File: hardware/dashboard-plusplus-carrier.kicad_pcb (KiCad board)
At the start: 4 copper layers, 95 x 55 mm, 54 parts, among them J1 XT30U-M, J10a ESP32-DEVKIT-A, J10b ESP32-DEVKIT-B, J13 DEBUG, J14 TRIP + EN, J15 SPARE, J17 IGN + COOLANT, J3 TFT-ILI9488, J6 LDR + FUEL, J8 GPS_PADS, J9 HALL, Q1 IRFR9540N, U4 DPP_DCDC_MODULE

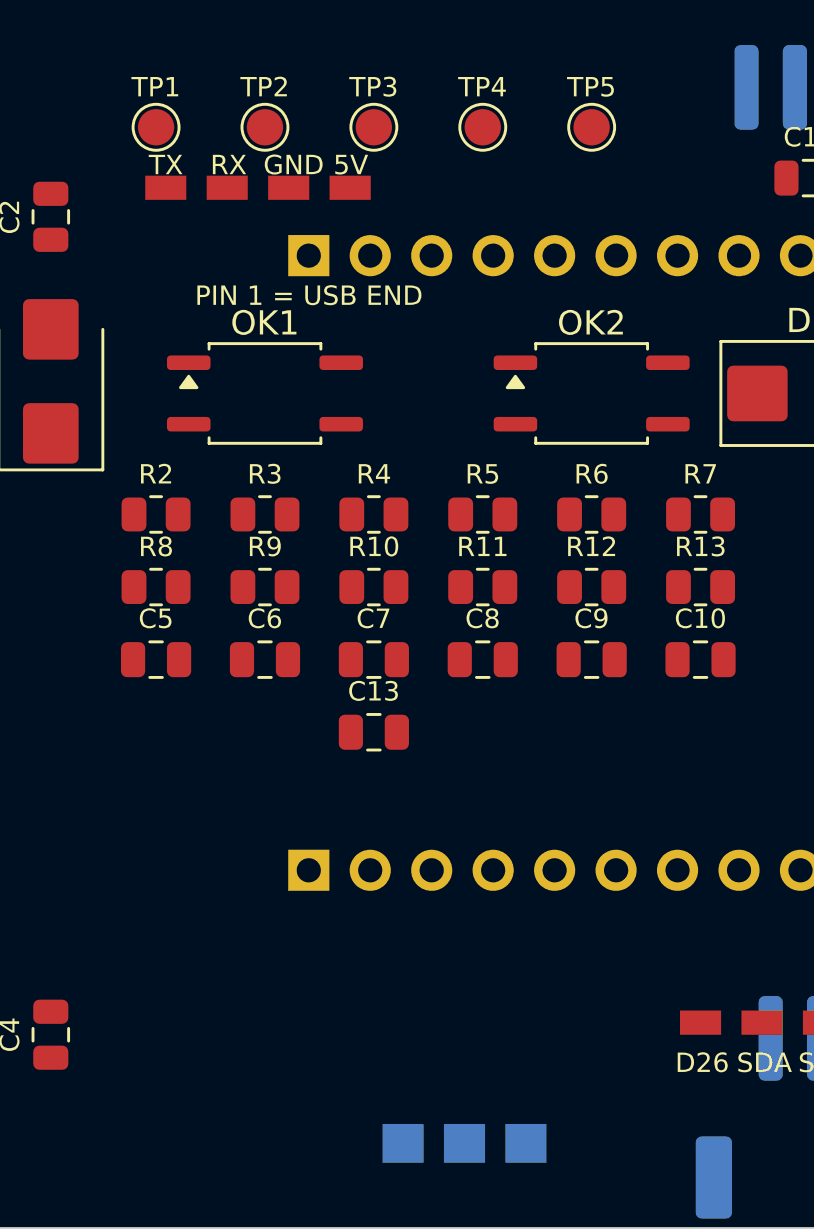
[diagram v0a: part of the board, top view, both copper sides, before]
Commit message: Move the debug TX/RX/GND/5V pads to the spare row by D26
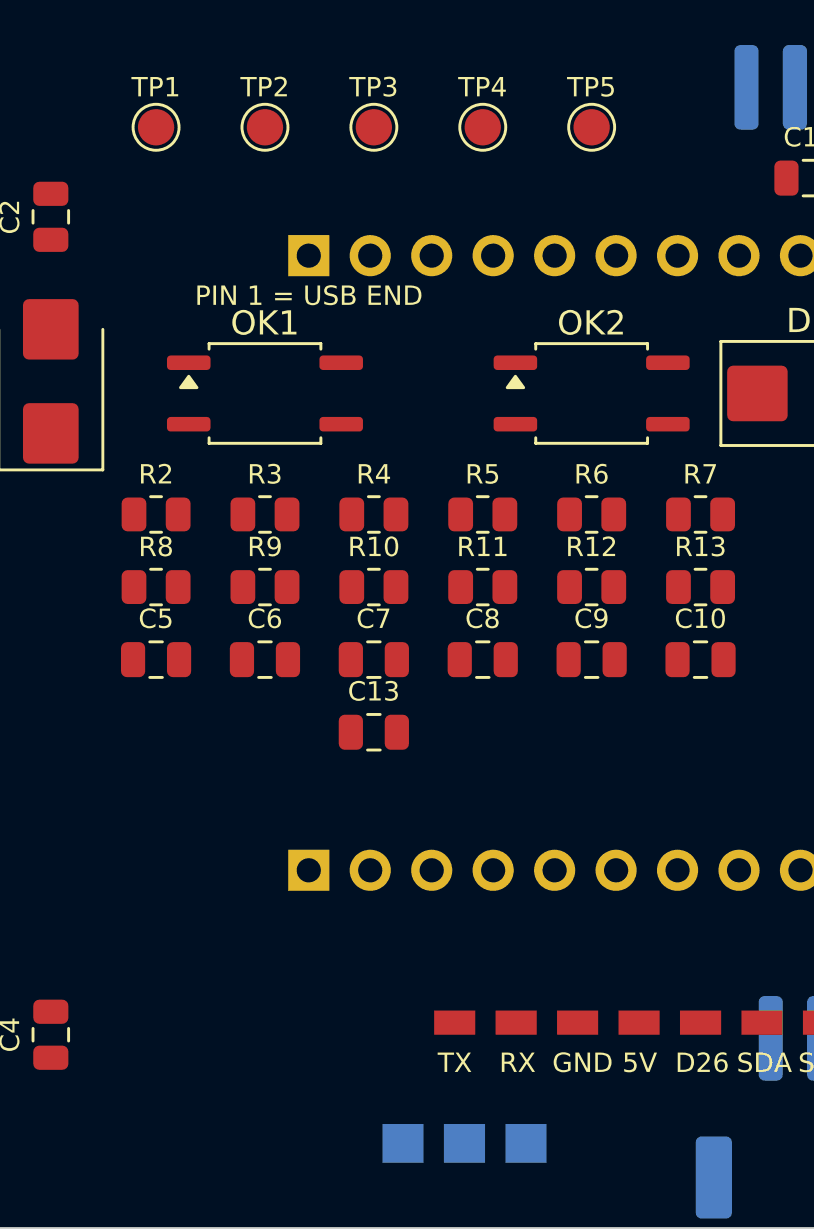
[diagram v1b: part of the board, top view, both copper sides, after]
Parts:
- moved J13 36.5 mm to (152.9, 124.0)
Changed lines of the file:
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@@
 (footprint "dpp:DEBUG"
 	(layer "F.Cu")
-	(at 141.0000 89.5000 0.0)
+	(at 152.9400 124.0000 0.0)
 	(property "Reference" "J13" (at 0.00 -1.30 0.0) (layer "F.Fab") (effects (font (size 1.0 1.0) (thickness 0.15))))
 	(property "Value" "DEBUG" (at 0.00 1.30 0.0) (layer "F.Fab") (effects (font (size 1.0 1.0) (thickness 0.15))))
@@
 (gr_text "SEL" (at 154.39 126.39 0.0) (layer "B.SilkS") (effects (font (size 0.80 0.80) (thickness 0.12)) (justify left top mirror)))
 (gr_text "12V" (at 156.94 126.39 0.0) (layer "B.SilkS") (effects (font (size 0.80 0.80) (thickness 0.12)) (justify left top mirror)))
-(gr_text "TX" (at 140.30 88.10 0.0) (layer "F.SilkS") (effects (font (size 0.80 0.80) (thickness 0.12)) (justify left top)))
-(gr_text "RX" (at 142.84 88.10 0.0) (layer "F.SilkS") (effects (font (size 0.80 0.80) (thickness 0.12)) (justify left top)))
-(gr_text "GND" (at 145.03 88.10 0.0) (layer "F.SilkS") (effects (font (size 0.80 0.80) (thickness 0.12)) (justify left top)))
-(gr_text "5V" (at 147.92 88.10 0.0) (layer "F.SilkS") (effects (font (size 0.80 0.80) (thickness 0.12)) (justify left top)))
+(gr_text "TX" (at 152.24 125.20 0.0) (layer "F.SilkS") (effects (font (size 0.80 0.80) (thickness 0.12)) (justify left top)))
+(gr_text "RX" (at 154.78 125.20 0.0) (layer "F.SilkS") (effects (font (size 0.80 0.80) (thickness 0.12)) (justify left top)))
+(gr_text "GND" (at 156.97 125.20 0.0) (layer "F.SilkS") (effects (font (size 0.80 0.80) (thickness 0.12)) (justify left top)))
+(gr_text "5V" (at 159.86 125.20 0.0) (layer "F.SilkS") (effects (font (size 0.80 0.80) (thickness 0.12)) (justify left top)))
 (gr_text "D26" (at 162.05 125.20 0.0) (layer "F.SilkS") (effects (font (size 0.80 0.80) (thickness 0.12)) (justify left top)))
 (gr_text "SDA" (at 164.59 125.20 0.0) (layer "F.SilkS") (effects (font (size 0.80 0.80) (thickness 0.12)) (justify left top)))

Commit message: Put the test-point row on the XT30 pad line (y 13.99)
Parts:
- moved TP1 5.51 mm to (140.6, 81.5)
- moved TP2 5.51 mm to (145.1, 81.5)
- moved TP3 5.51 mm to (149.6, 81.5)
- moved TP4 5.51 mm to (154.1, 81.5)
- moved TP5 5.51 mm to (158.6, 81.5)
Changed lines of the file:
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@@
 (footprint "dpp:TestPoint_Pad_D1.5mm"
 	(layer "F.Cu")
-	(at 140.6000 87.0000 0.0)
+	(at 140.6000 81.4900 0.0)
 (descr "SMD pad as test Point, diameter 1.5mm")
 (tags "test point SMD pad")
@@
 (footprint "dpp:TestPoint_Pad_D1.5mm"
 	(layer "F.Cu")
-	(at 145.1000 87.0000 0.0)
+	(at 145.1000 81.4900 0.0)
 (descr "SMD pad as test Point, diameter 1.5mm")
 (tags "test point SMD pad")
@@
 (footprint "dpp:TestPoint_Pad_D1.5mm"
 	(layer "F.Cu")
-	(at 149.6000 87.0000 0.0)
+	(at 149.6000 81.4900 0.0)
 (descr "SMD pad as test Point, diameter 1.5mm")
 (tags "test point SMD pad")
@@
 (footprint "dpp:TestPoint_Pad_D1.5mm"
 	(layer "F.Cu")
-	(at 154.1000 87.0000 0.0)
+	(at 154.1000 81.4900 0.0)
 (descr "SMD pad as test Point, diameter 1.5mm")
 (tags "test point SMD pad")
@@
 (footprint "dpp:TestPoint_Pad_D1.5mm"
 	(layer "F.Cu")
-	(at 158.6000 87.0000 0.0)
-(descr "SMD pad as test Point, diameter 1.5mm")
-(tags "test point SMD pad")
+	(at 158.6000 81.4900 0.0)
+(descr "SMD pad as test Point, diameter 1.5mm")
+(tags "test point SMD pad")

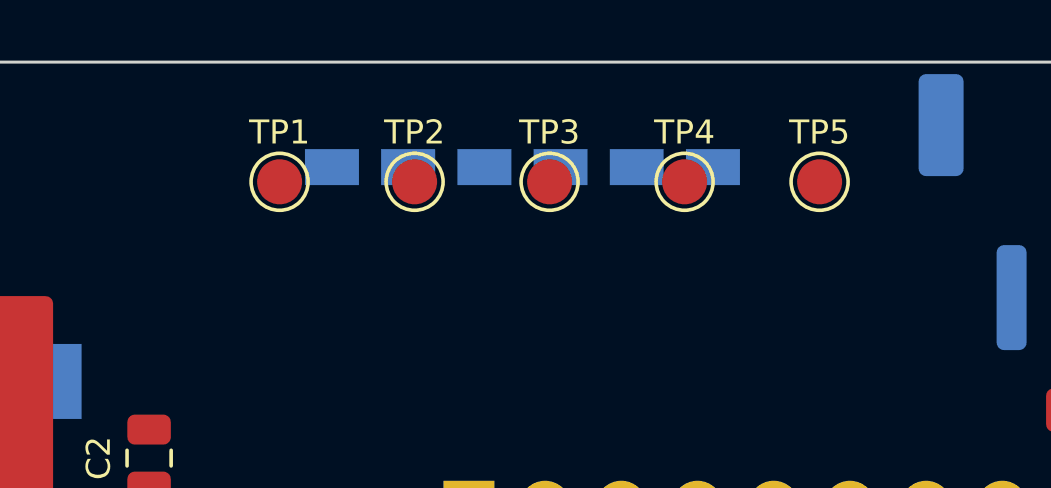
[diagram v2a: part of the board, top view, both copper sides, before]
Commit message: Label the test points with their nets, caption row TEST PROBES
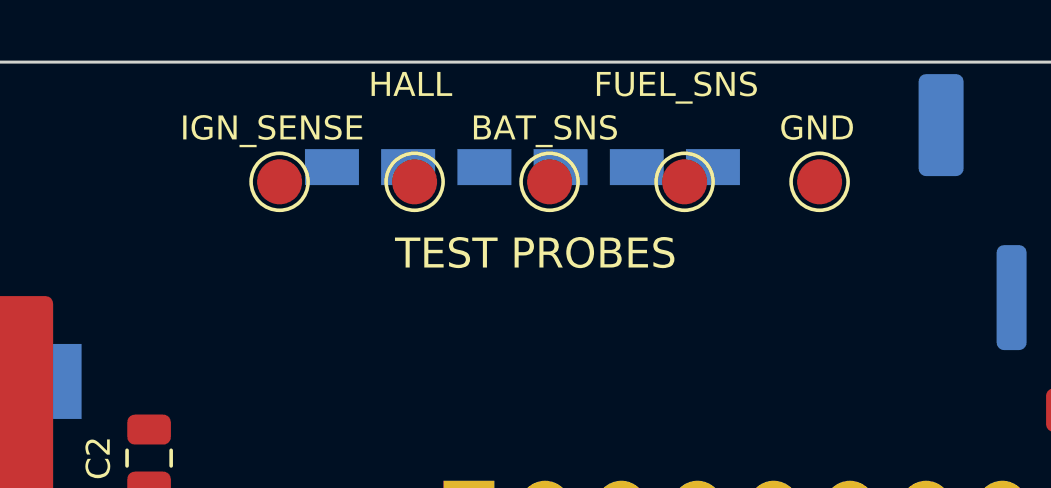
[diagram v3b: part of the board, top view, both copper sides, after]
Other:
- board text added: "BAT_SNS"
- board text added: "FUEL_SNS"
- board text added: "IGN_SENSE"
- board text added: "TEST PROBES"
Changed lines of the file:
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@@
 (property "Reference" "TP1"
 		(at 0 -1.648 0)
-		(layer "F.SilkS")
-		(effects
-			(font
-				(size 0.80 0.80)
-				(thickness 0.12)
+		(layer "F.Fab")
+		(effects
+			(font
+				(size 1 1)
+				(thickness 0.15)
 			)
 		)
@@
 (property "Reference" "TP2"
 		(at 0 -1.648 0)
-		(layer "F.SilkS")
-		(effects
-			(font
-				(size 0.80 0.80)
-				(thickness 0.12)
+		(layer "F.Fab")
+		(effects
+			(font
+				(size 1 1)
+				(thickness 0.15)
 			)
 		)
@@
 (property "Reference" "TP3"
 		(at 0 -1.648 0)
-		(layer "F.SilkS")
-		(effects
-			(font
-				(size 0.80 0.80)
-				(thickness 0.12)
+		(layer "F.Fab")
+		(effects
+			(font
+				(size 1 1)
+				(thickness 0.15)
 			)
 		)
@@
 (property "Reference" "TP4"
 		(at 0 -1.648 0)
-		(layer "F.SilkS")
-		(effects
-			(font
-				(size 0.80 0.80)
-				(thickness 0.12)
+		(layer "F.Fab")
+		(effects
+			(font
+				(size 1 1)
+				(thickness 0.15)
 			)
 		)
@@
 (property "Reference" "TP5"
 		(at 0 -1.648 0)
-		(layer "F.SilkS")
-		(effects
-			(font
-				(size 0.80 0.80)
-				(thickness 0.12)
+		(layer "F.Fab")
+		(effects
+			(font
+				(size 1 1)
+				(thickness 0.15)
 			)
 		)
@@
 (gr_text "HALL" (at 169.41 120.40 0.0) (layer "B.SilkS") (effects (font (size 0.80 0.80) (thickness 0.12)) (justify left top mirror)))
 (gr_text "GNSS" (at 160.00 80.40 0.0) (layer "B.SilkS") (effects (font (size 0.80 0.80) (thickness 0.12)) (justify left top mirror)))
+(gr_text "IGN_SENSE" (at 137.28 79.24 0.0) (layer "F.SilkS") (effects (font (size 0.80 0.80) (thickness 0.12)) (justify left top)))
+(gr_text "HALL" (at 143.56 77.79 0.0) (layer "F.SilkS") (effects (font (size 0.80 0.80) (thickness 0.12)) (justify left top)))
+(gr_text "BAT_SNS" (at 146.97 79.24 0.0) (layer "F.SilkS") (effects (font (size 0.80 0.80) (thickness 0.12)) (justify left top)))
+(gr_text "FUEL_SNS" (at 151.07 77.79 0.0) (layer "F.SilkS") (effects (font (size 0.80 0.80) (thickness 0.12)) (justify left top)))
+(gr_text "GND" (at 157.26 79.24 0.0) (layer "F.SilkS") (effects (font (size 0.80 0.80) (thickness 0.12)) (justify left top)))
+(gr_text "TEST PROBES" (at 144.45 83.30 0.0) (layer "F.SilkS") (effects (font (size 1.00 1.00) (thickness 0.15)) (justify left top)))
 (gr_text "SDA" (at 143.39 82.90 0.0) (layer "B.SilkS") (effects (font (size 0.80 0.80) (thickness 0.12)) (justify left top mirror)))
 (gr_text "SCL" (at 145.94 82.90 0.0) (layer "B.SilkS") (effects (font (size 0.80 0.80) (thickness 0.12)) (justify left top mirror)))

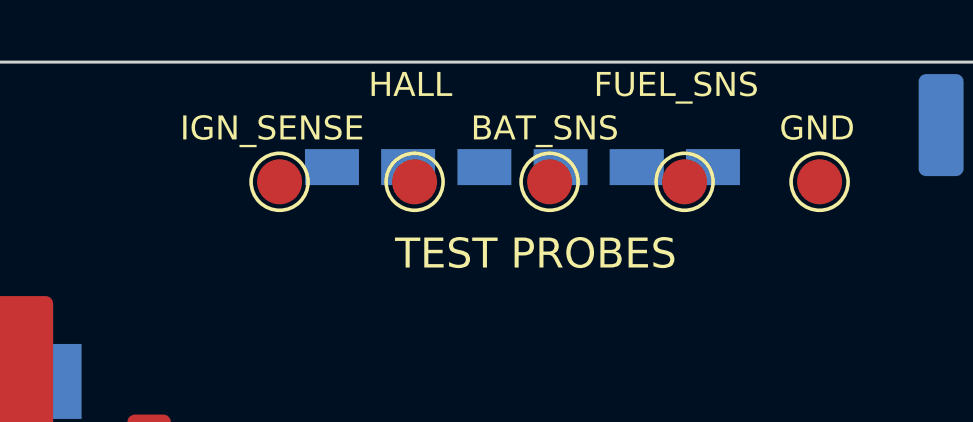
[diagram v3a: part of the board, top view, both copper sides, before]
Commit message: Shorten test-point silks to IGN HALL BAT FUEL GND on one line
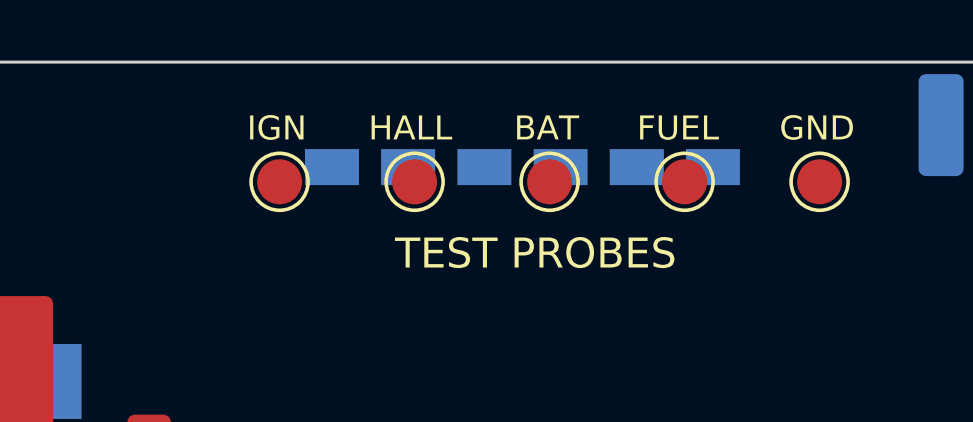
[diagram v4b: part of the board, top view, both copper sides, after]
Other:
- board text added: "BAT"
- board text added: "their silks read out short forms: IGN HALL BAT FUEL GND"
- board text removed: "BAT_SNS"
- board text removed: "FUEL_SNS"
- board text removed: "IGN_SENSE"
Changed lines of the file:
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@@
 (gr_text "HALL" (at 169.41 120.40 0.0) (layer "B.SilkS") (effects (font (size 0.80 0.80) (thickness 0.12)) (justify left top mirror)))
 (gr_text "GNSS" (at 160.00 80.40 0.0) (layer "B.SilkS") (effects (font (size 0.80 0.80) (thickness 0.12)) (justify left top mirror)))
-(gr_text "IGN_SENSE" (at 137.28 79.24 0.0) (layer "F.SilkS") (effects (font (size 0.80 0.80) (thickness 0.12)) (justify left top)))
-(gr_text "HALL" (at 143.56 77.79 0.0) (layer "F.SilkS") (effects (font (size 0.80 0.80) (thickness 0.12)) (justify left top)))
-(gr_text "BAT_SNS" (at 146.97 79.24 0.0) (layer "F.SilkS") (effects (font (size 0.80 0.80) (thickness 0.12)) (justify left top)))
-(gr_text "FUEL_SNS" (at 151.07 77.79 0.0) (layer "F.SilkS") (effects (font (size 0.80 0.80) (thickness 0.12)) (justify left top)))
+(gr_text "IGN" (at 139.51 79.24 0.0) (layer "F.SilkS") (effects (font (size 0.80 0.80) (thickness 0.12)) (justify left top)))
+(gr_text "HALL" (at 143.56 79.24 0.0) (layer "F.SilkS") (effects (font (size 0.80 0.80) (thickness 0.12)) (justify left top)))
+(gr_text "BAT" (at 148.41 79.24 0.0) (layer "F.SilkS") (effects (font (size 0.80 0.80) (thickness 0.12)) (justify left top)))
+(gr_text "FUEL" (at 152.51 79.24 0.0) (layer "F.SilkS") (effects (font (size 0.80 0.80) (thickness 0.12)) (justify left top)))
 (gr_text "GND" (at 157.26 79.24 0.0) (layer "F.SilkS") (effects (font (size 0.80 0.80) (thickness 0.12)) (justify left top)))
 (gr_text "TEST PROBES" (at 144.45 83.30 0.0) (layer "F.SilkS") (effects (font (size 1.00 1.00) (thickness 0.15)) (justify left top)))
@@
 (gr_text "J13 DEBUG  J15 SPARE (D26 SDA SCL D19 D15 GND)" (at 111.50 155.90 0.0) (layer "Dwgs.User") (effects (font (size 1.00 1.00) (thickness 0.12)) (justify left top)))
 (gr_text "TP1 IGN_SENSE  TP2 HALL  TP3 BAT_SNS  TP4 FUEL_SNS  TP5 GND" (at 111.50 157.40 0.0) (layer "Dwgs.User") (effects (font (size 1.00 1.00) (thickness 0.12)) (justify left top)))
+(gr_text "their silks read out short forms: IGN HALL BAT FUEL GND" (at 111.50 158.90 0.0) (layer "Dwgs.User") (effects (font (size 1.00 1.00) (thickness 0.12)) (justify left top)))
 (zone (net 0) (net_name "") (layer "F.Cu") (hatch edge 0.5) (keepout (tracks not_allowed) (vias not_allowed) (pads not_allowed) (copperpour not_allowed)) (polygon (pts (xy 173.87 94.30) (xy 187.80 94.30) (xy 187.80 115.70) (xy 173.87 115.70) (xy 173.87 94.30))))
 (zone (net 0) (net_name "") (layer "B.Cu") (hatch edge 0.5) (keepout (tracks not_allowed) (vias not_allowed) (pads not_allowed) (copperpour not_allowed)) (polygon (pts (xy 173.87 94.30) (xy 187.80 94.30) (xy 187.80 115.70) (xy 173.87 115.70) (xy 173.87 94.30))))

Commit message: Move Q1 F1 D1 R1 4.10 mm south, shift D2's silk label clear
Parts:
- moved D1 4.10 mm to (114.3, 92.3)
- moved R1 4.10 mm to (114.3, 97.3)
- moved F1 4.10 mm to (121.2, 120.2)
- moved Q1 4.10 mm to (126.8, 94.8)
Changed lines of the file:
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@@
 (footprint "dpp:Fuseholder_Clip-5x20mm_Littelfuse_521_Lateral_P17.00x5.00mm_D1.30mm_Horizontal"
 	(layer "F.Cu")
-	(at 121.2500 116.1400 90.0)
+	(at 121.2500 120.2400 90.0)
 (descr "Fuseholder Clips, 5x20mm Cylinder Fuse, Pins Inline, Horizontal, Littelfuse 521, https://www.littelfuse.com/~/media/electronics/datasheets/fuse_clips/littelfuse_fuse_clip_520_521_102071_datasheet.pdf.pdf")
 (tags "fuse clip open")
@@
 (footprint "dpp:TO-263-3_TabPin2"
 	(layer "F.Cu")
-	(at 126.8500 90.7000 0.0)
+	(at 126.8500 94.8000 0.0)
 (descr "TO-263/D2PAK/DDPAK SMD package, http://www.infineon.com/cms/en/product/packages/PG-TO263/PG-TO263-3-1/")
 (tags "D2PAK DDPAK TO-263 D2PAK-3 TO-263-3 SOT-404")
@@
 (footprint "dpp:D_SOD-123"
 	(layer "F.Cu")
-	(at 114.3000 88.1600 270.0)
+	(at 114.3000 92.2600 270.0)
 (descr "SOD-123")
 (tags "SOD-123")
@@
 (tags "Diode SMB (DO-214AA)")
 (property "Reference" "D2"
-		(at 0 -3 90)
+		(at -5.90 0.00 90)
 		(layer "F.SilkS")
 		(effects
@@
 (footprint "dpp:R_0805_2012Metric"
 	(layer "F.Cu")
-	(at 114.3000 93.2400 270.0)
+	(at 114.3000 97.3400 270.0)
 (descr "Resistor SMD 0805 (2012 Metric), square (rectangular) end terminal, IPC-7351 nominal, (Body size source: IPC-SM-782 page 72, https://www.pcb-3d.com/wordpress/wp-content/uploads/ipc-sm-782a_amendment_1_and_2.pdf)")
 (tags "resistor")
